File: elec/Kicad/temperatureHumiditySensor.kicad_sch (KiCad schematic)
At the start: 0 parts

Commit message: sa progresse. Battery management fini + humidity/temp sensor + bouton
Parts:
- added C9: 100nF, symbol Device:C
- added U4: HTU21D, HTU21D:QFN100P300X300X100-7N, symbol HTU21D:HTU21D
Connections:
- new net: C9.2, U4.2 (GND), U4.PAD (GND)
- new net +3.3V: C9.1, U4.5 (VDD)
- new net I2C1_SCL: U4.6 (SCK)
- new net I2C1_SDA: U4.1 (DATA)
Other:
- note added: "I2C address=0x40"
- note added: "Mettre des pull-up resistor sur la ligne I2C dans la schématique du MCU (Fait)"

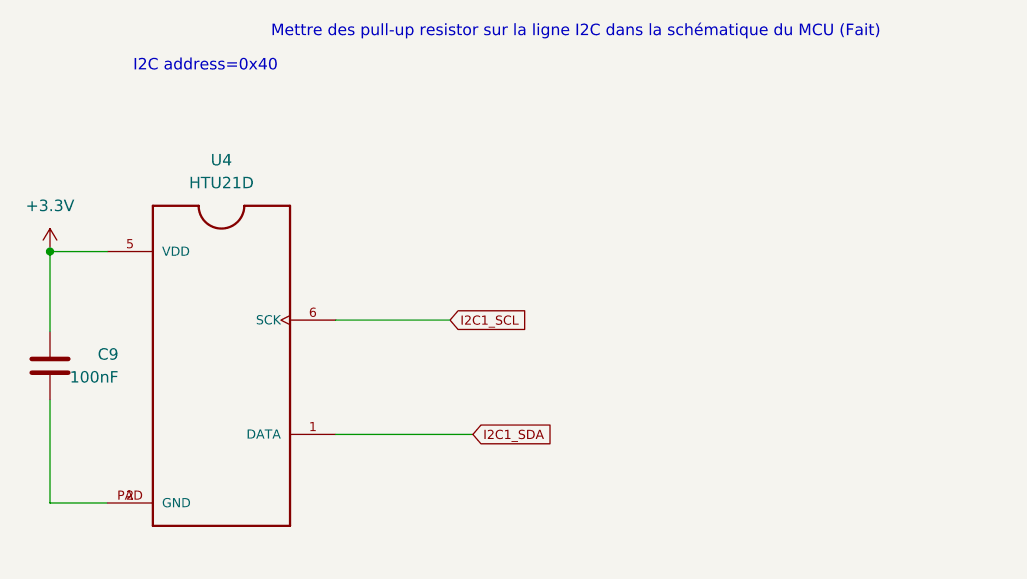
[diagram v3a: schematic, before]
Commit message: add a few footprint
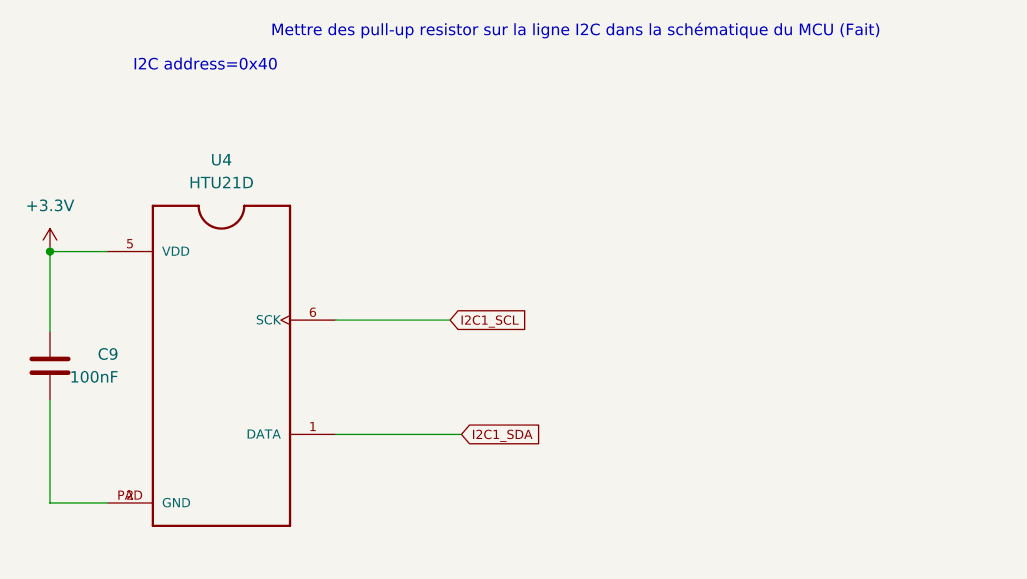
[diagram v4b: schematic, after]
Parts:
- C9: footprint (none) -> Capacitor_SMD:C_0603_1608Metric_Pad1.08x0.95mm_HandSolder
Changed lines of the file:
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@@
 	(wire
 		(pts
-			(xy 149.86 80.01) (xy 165.1 80.01)
+			(xy 149.86 80.01) (xy 163.83 80.01)
 		)
 		(stroke
@@
 	(global_label "I2C1_SDA"
 		(shape input)
-		(at 165.1 80.01 0)
+		(at 163.83 80.01 0)
 		(fields_autoplaced yes)
 		(effects
@@
 		)
 		(property "Intersheetrefs" "${INTERSHEET_REFS}"
-			(at 174.5515 80.01 0)
+			(at 173.2815 80.01 0)
 			(effects
 				(font
@@
 			)
 		)
-		(property "Footprint" ""
+		(property "Footprint" "Capacitor_SMD:C_0603_1608Metric_Pad1.08x0.95mm_HandSolder"
 			(at 117.1448 76.2 0)
 			(effects
@@
 			)
 		)
-		(property "Datasheet" "https://www.digikey.ca/en/products/detail/tdk-corporation/C2012X7S1A226M125AC/3951796"
+		(property "Datasheet" "https://www.digikey.ca/en/products/detail/yageo/CC0603KRX7R7BB104/302822"
 			(at 118.11 72.39 0)
 			(effects

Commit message: Jpense pas boire jeudi sérieux vue que y'a pas de 5@8
routage du découplage et des CLK
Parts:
- C9: footprint Capacitor_SMD:C_0603_1608Metric_Pad1.08x0.95mm_HandSolder -> Capacitor_SMD:C_0402_1005Metric_Pad0.74x0.62mm_HandSolder
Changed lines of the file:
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@@
 			)
 		)
-		(property "Footprint" "Capacitor_SMD:C_0603_1608Metric_Pad1.08x0.95mm_HandSolder"
+		(property "Footprint" "Capacitor_SMD:C_0402_1005Metric_Pad0.74x0.62mm_HandSolder"
 			(at 117.1448 76.2 0)
 			(effects

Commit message: sorry Jacob tu va être dessus ...
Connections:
- net GND: now reaches C9.2, U4.2 (GND), U4.PAD (GND)
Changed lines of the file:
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@@
 	(paper "A4")
+	(junction
+		(at 118.11 87.63)
+		(diameter 0)
+		(color 0 0 0 0)
+	)
 	(junction
 		(at 118.11 59.69)
@@
 			)
 		)
+	)
+	(symbol
+		(lib_id "power:GND")
+		(at 118.11 87.63 0)
+		(unit 1)
+		(exclude_from_sim no)
+		(in_bom yes)
+		(on_board yes)
+		(dnp no)
+		(fields_autoplaced yes)
+		(property "Reference" "#PWR09"
+			(at 118.11 93.98 0)
+			(effects
+				(font
+					(size 1.27 1.27)
+				)
+				(hide yes)
+			)
+		)
+		(property "Value" "GND"
+			(at 118.11 92.71 0)
+			(effects
+				(font
+					(size 1.27 1.27)
+				)
+			)
+		)
+		(property "Footprint" ""
+			(at 118.11 87.63 0)
+			(effects
+				(font
+					(size 1.27 1.27)
+				)
+				(hide yes)
+			)
+		)
+		(property "Datasheet" ""
+			(at 118.11 87.63 0)
+			(effects
+				(font
+					(size 1.27 1.27)
+				)
+				(hide yes)
+			)
+		)
+		(property "Description" "Power symbol creates a global label with name \"GND\" , ground"
+			(at 118.11 87.63 0)
+			(effects
+				(font
+					(size 1.27 1.27)
+				)
+				(hide yes)
+			)
+		)
+		(pin "1"
+		)
+		(instances
+			(project ""
+				(path "/a1545928-1195-40b9-b3c4-78f837012afb/4cc0ebdd-0f2a-405e-9a30-83f437855272"
+					(reference "#PWR09")
+					(unit 1)
+				)
+			)
+		)
